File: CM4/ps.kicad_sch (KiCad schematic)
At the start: 42 parts, among them J1 USB_B, J2 Conn_01x02, J3 Conn_01x02, Q1 EMH3, U3 BQ25887RGET, U4 MAX17643, U5 ATTINY85-20PU, U6 TQ2SA-L2-3V-Z-Remake

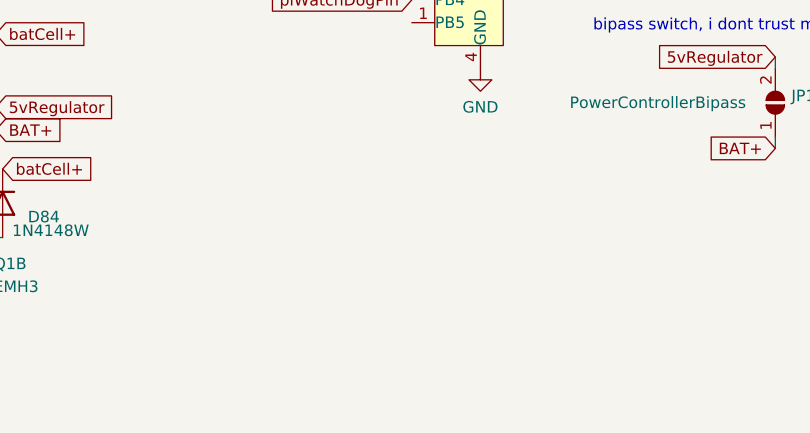
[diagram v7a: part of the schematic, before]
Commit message: Added high current 3.3v supply
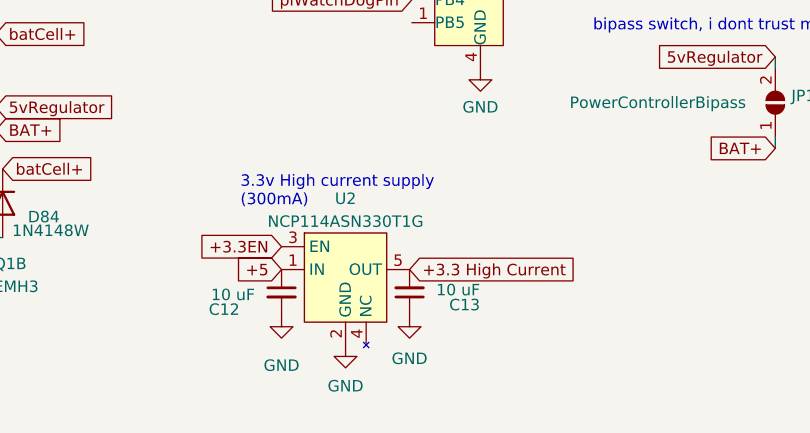
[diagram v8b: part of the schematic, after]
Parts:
- added C12, C13: 10 uF, Capacitor_SMD:C_1206_3216Metric, symbol Device:C_Small
- added U2: NCP114ASN330T1G, Package_TO_SOT_SMD:TSOT-23-5_HandSoldering, symbol teensy:NCP114ASN330T1G
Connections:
- net +5: now also C12.1, U2.1 (IN)
- net GND: now also C12.2, C13.1, U2.2 (GND)
- new net +3.3 High Current: C13.2, U2.5 (OUT)
- new net +3.3EN: U2.3 (EN)
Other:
- note added: "3.3v High current supply (300mA)"
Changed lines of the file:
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@@
     (stroke (width 0) (type dash) (color 0 0 0 0))
   )
-  (image (at 66.04 151.765)
+  (image (at 32.766 104.267) (scale 0.387142)
     (data
       iVBORw0KGgoAAAANSUhEUgAAA6gAAAMTCAMAAACbksqsAAAAA3NCSVQICAjb4U/gAAABX1BMVEX/
@@
     (effects (font (size 1.27 1.27)) (justify right bottom))
   )
+  (text "3.3v High current supply\n(300mA)" (at 198.882 141.986 0)
+    (effects (font (size 1.27 1.27)) (justify left bottom))
+  )
   (text "Power Control" (at 205.74 99.695 180)
     (effects (font (size 1.27 1.27)) (justify right bottom))
@@
     )
   )
+  (global_label "+3.3EN" (shape input) (at 203.454 146.304 180)
+    (effects (font (size 1.27 1.27)) (justify right))
+    (property "Intersheet References" "${INTERSHEET_REFS}" (id 0) (at 193.9652 146.2246 0)
+      (effects (font (size 1.27 1.27)) (justify right) hide)
+    )
+  )
+  (global_label "+5" (shape input) (at 203.454 148.844 180)
+    (effects (font (size 1.27 1.27)) (justify right))
+    (property "Intersheet References" "${INTERSHEET_REFS}" (id 0) (at 198.259 148.7646 0)
+      (effects (font (size 1.27 1.27)) (justify right) hide)
+    )
+  )
+  (global_label "+3.3 High Current" (shape input) (at 217.678 148.844 0)
+    (effects (font (size 1.27 1.27)) (justify left))
+    (property "Intersheet References" "${INTERSHEET_REFS}" (id 0) (at 237.8106 148.7646 0)
+      (effects (font (size 1.27 1.27)) (justify left) hide)
+    )
+  )
   (global_label "SetPowerON" (shape input) (at 217.932 113.792 180)
     (effects (font (size 1.27 1.27)) (justify right))
@@
     (pin "1")
   )
+  (symbol (lib_id "power:GND") (at 203.454 153.924 0) (unit 1)
+    (in_bom yes) (on_board yes)
+    (property "Reference" "#PWR0132" (id 0) (at 203.454 160.274 0)
+      (effects (font (size 1.27 1.27)) hide)
+    )
+    (property "Value" "GND" (id 1) (at 203.454 159.512 0))
+    (property "Footprint" "" (id 2) (at 203.454 153.924 0)
+      (effects (font (size 1.27 1.27)) hide)
+    )
+    (property "Datasheet" "" (id 3) (at 203.454 153.924 0)
+      (effects (font (size 1.27 1.27)) hide)
+    )
+    (pin "1")
+  )
   (symbol (lib_id "power:GND") (at 208.28 57.15 0) (unit 1)
     (in_bom yes) (on_board yes)
@@
     )
     (property "Datasheet" "" (id 3) (at 208.28 57.15 0)
+      (effects (font (size 1.27 1.27)) hide)
+    )
+    (pin "1")
+  )
+  (symbol (lib_id "power:GND") (at 210.566 157.226 0) (unit 1)
+    (in_bom yes) (on_board yes)
+    (property "Reference" "#PWR0131" (id 0) (at 210.566 163.576 0)
+      (effects (font (size 1.27 1.27)) hide)
+    )
+    (property "Value" "GND" (id 1) (at 210.566 161.798 0))
+    (property "Footprint" "" (id 2) (at 210.566 157.226 0)
+      (effects (font (size 1.27 1.27)) hide)
+    )
+    (property "Datasheet" "" (id 3) (at 210.566 157.226 0)
+      (effects (font (size 1.27 1.27)) hide)
+    )
+    (pin "1")
+  )
+  (symbol (lib_id "power:GND") (at 217.678 153.924 0) (unit 1)
+    (in_bom yes) (on_board yes)
+    (property "Reference" "#PWR0133" (id 0) (at 217.678 160.274 0)
+      (effects (font (size 1.27 1.27)) hide)
+    )
+    (property "Value" "GND" (id 1) (at 217.678 158.75 0))
+    (property "Footprint" "" (id 2) (at 217.678 153.924 0)
+      (effects (font (size 1.27 1.27)) hide)
+    )
+    (property "Datasheet" "" (id 3) (at 217.678 153.924 0)
       (effects (font (size 1.27 1.27)) hide)
     )
@@
     (pin "2")
   )
+  (symbol (lib_id "Device:C_Small") (at 203.454 151.384 0) (unit 1)
+    (in_bom yes) (on_board yes)
+    (property "Reference" "C12" (id 0) (at 195.3642 153.2901 0)
+      (effects (font (size 1.27 1.27)) (justify left))
+    )
+    (property "Value" "10 uF" (id 1) (at 195.6182 151.6518 0)
+      (effects (font (size 1.27 1.27)) (justify left))
+    )
+    (property "Footprint" "Capacitor_SMD:C_1206_3216Metric" (id 2) (at 203.454 151.384 0)
+      (effects (font (size 1.27 1.27)) hide)
+    )
+    (property "Datasheet" "~" (id 3) (at 203.454 151.384 0)
+      (effects (font (size 1.27 1.27)) hide)
+    )
+    (pin "1")
+    (pin "2")
+  )
+  (symbol (lib_id "Device:C_Small") (at 217.678 151.384 180) (unit 1)
+    (in_bom yes) (on_board yes)
+    (property "Reference" "C13" (id 0) (at 225.5138 152.7799 0)
+      (effects (font (size 1.27 1.27)) (justify left))
+    )
+    (property "Value" "10 uF" (id 1) (at 225.5138 151.1162 0)
+      (effects (font (size 1.27 1.27)) (justify left))
+    )
+    (property "Footprint" "Capacitor_SMD:C_1206_3216Metric" (id 2) (at 217.678 151.384 0)
+      (effects (font (size 1.27 1.27)) hide)
+    )
+    (property "Datasheet" "~" (id 3) (at 217.678 151.384 0)
+      (effects (font (size 1.27 1.27)) hide)
+    )
+    (pin "1")
+    (pin "2")
+  )
   (symbol (lib_id "Device:C_Small") (at 220.98 55.245 0) (unit 1)
     (in_bom yes) (on_board yes)
@@
     (pin "3")
     (pin "4")
+    (pin "5")
+  )
+  (symbol (lib_id "teensy:NCP114ASN330T1G") (at 210.566 148.59 0) (unit 1)
+    (in_bom yes) (on_board yes)
+    (property "Reference" "U2" (id 0) (at 210.566 140.97 0))
+    (property "Value" "NCP114ASN330T1G" (id 1) (at 210.566 143.51 0))
+    (property "Footprint" "Package_TO_SOT_SMD:TSOT-23-5_HandSoldering" (id 2) (at 193.802 160.782 0)
+      (effects (font (size 1.27 1.27)) hide)
+    )
+    (property "Datasheet" "" (id 3) (at 193.802 160.782 0)
+      (effects (font (size 1.27 1.27)) hide)
+    )
+    (pin "1")
+    (pin "2")
+    (pin "3")
+    (pin "4")
